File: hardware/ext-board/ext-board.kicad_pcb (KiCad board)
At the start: 2 copper layers, 38.5 x 85 mm, 24 parts, among them J1 GH BM07B link to INT, J2 VCC DATA GND, J3 PTSM 0,5/2-HH-2,5-THR 24 VAC, J4 5V OUT to Pi USB-C, U1 DS2482-100, U2 DS2482-100 (0x19), U3 TMR 12-4811WI

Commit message: Silkscreen: J6 reference below the header, the trunk label beside H1's pin letters
Co-Authored-By: Claude Fable 5.1 <noreply@anthropic.com>
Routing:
- net VCC: track 150.0 -> 177.9 mm, vias 3 -> 1
- net GND: track 167.1 -> 181.6 mm
- net ACR: track 54.0 -> 43.3 mm
- net DATA: track 146.1 -> 138.9 mm
- net GPIO4: track 40.9 -> 46.7 mm
- net SCL: track 74.4 -> 71.6 mm
- net SDA: track 75.1 -> 72.8 mm, vias 2 -> 0
- net H3_DATA: track 15.6 -> 17.5 mm
- net VS: track 72.6 -> 71.2 mm
- net COM: track 48.7 -> 47.7 mm, vias 0 -> 1
- net ACC: vias 1 -> 0
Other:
- board text added: "trunk"
- board text removed: "H1 trunk"

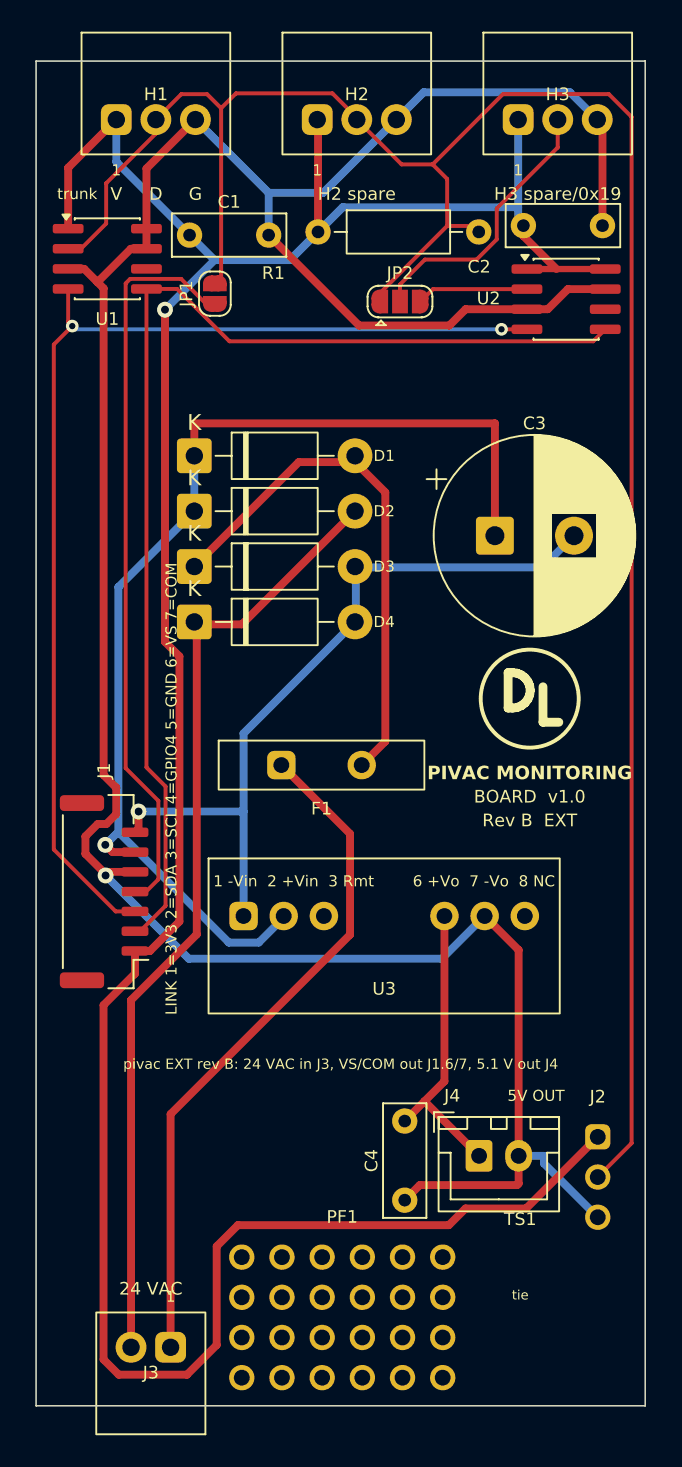
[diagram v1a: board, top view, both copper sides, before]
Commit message: EXT silkscreen: converter pins labelled one by one, R1's reference under R1, link legend beside J1
Co-Authored-By: Claude Fable 5.1 <noreply@anthropic.com>
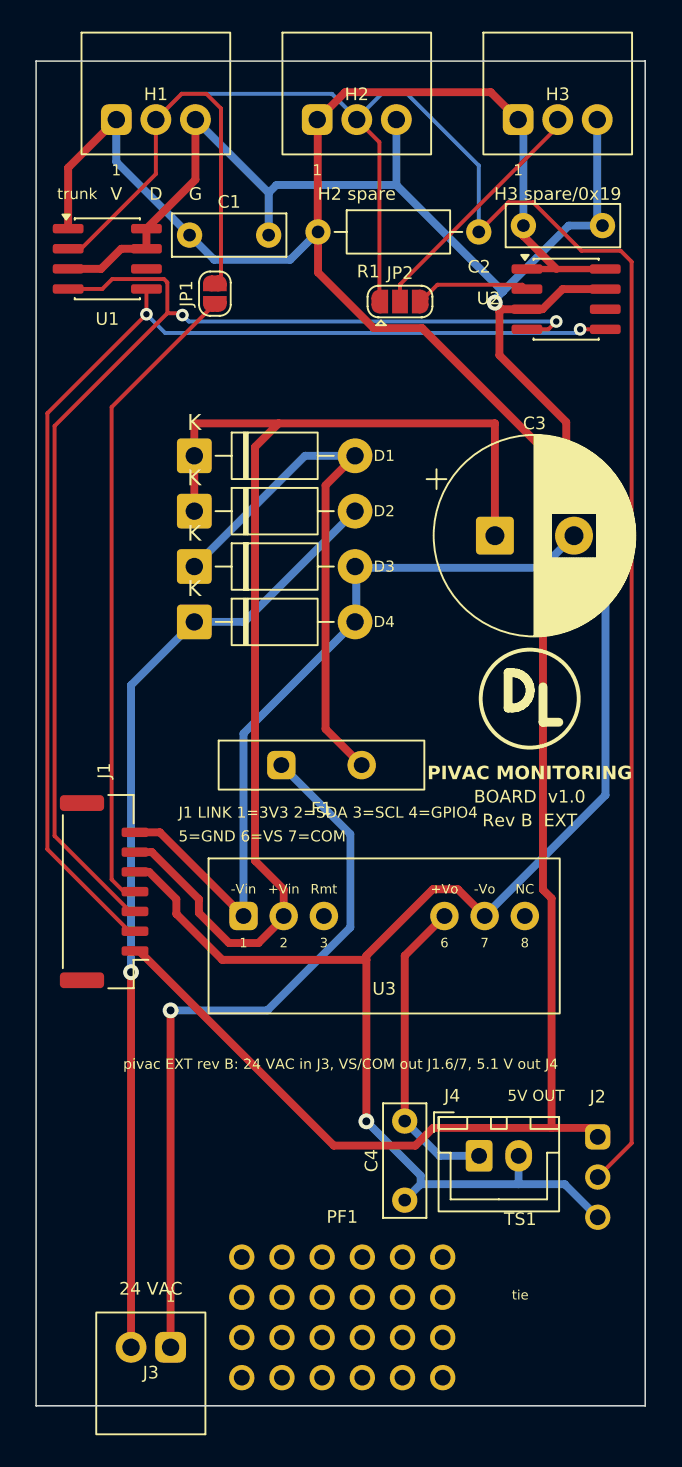
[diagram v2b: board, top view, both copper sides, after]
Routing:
- net VCC: track 177.9 -> 163.1 mm, vias 1 -> 0
- net GND: track 181.6 -> 172.3 mm, vias 1 -> 3
- net SCL: track 71.6 -> 78.5 mm
- net VS: track 71.2 -> 77.2 mm, vias 1 -> 0
- net GPIO4: track 46.7 -> 40.9 mm
- net ACR: track 43.3 -> 46.9 mm, vias 0 -> 1
- net SDA: track 72.8 -> 75.3 mm, vias 0 -> 2
- net H3_DATA: track 17.5 -> 15.6 mm
- net COM: track 47.7 -> 48.7 mm, vias 1 -> 0
- net +5V: track 18.9 -> 19.6 mm
- net ACC: vias 0 -> 1
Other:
- board text added: "5=GND 6=VS 7=COM"
- board text added: "J1 LINK 1=3V3 2=SDA 3=SCL 4=GPIO4"
- board text removed: "LINK 1=3V3 2=SDA 3=SCL 4=GPIO4 5=GND 6=VS 7=COM"

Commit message: EXT silkscreen: R1 and F1 references moved clear, link legend in three lines beside J1
Co-Authored-By: Claude Fable 5.1 <noreply@anthropic.com>
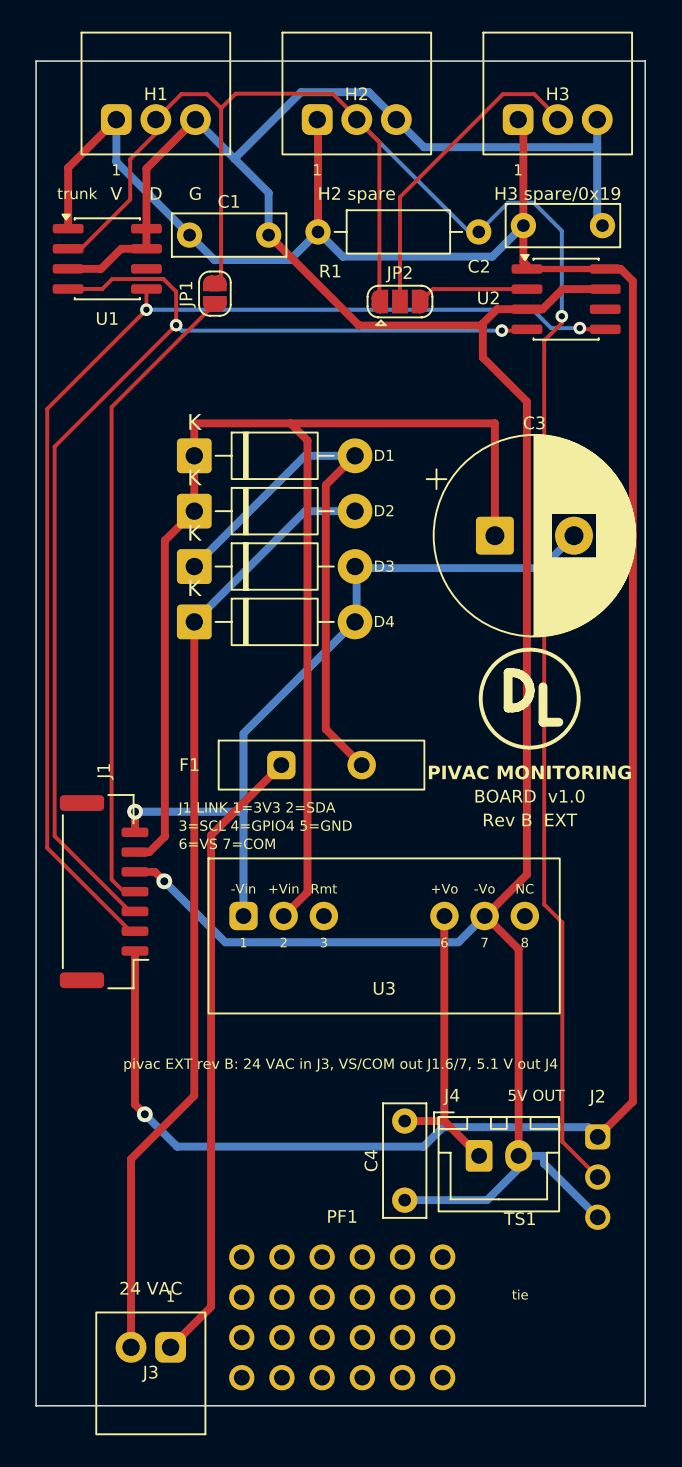
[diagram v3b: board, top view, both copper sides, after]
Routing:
- net DATA: track 138.7 -> 128.2 mm, vias 0 -> 1
- net VS: track 77.2 -> 87.5 mm
- net ACR: track 46.9 -> 39.7 mm, vias 1 -> 0
- net GND: track 172.3 -> 178.1 mm, vias 3 -> 1
- net H3_DATA: track 15.6 -> 20.0 mm
- net SCL: track 78.5 -> 74.4 mm
- net VCC: track 163.1 -> 161.0 mm, vias 0 -> 1
- net +5V: track 19.6 -> 18.6 mm
- net COM: track 48.7 -> 47.8 mm, vias 0 -> 1
- net ACC: vias 1 -> 0
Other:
- board text added: "3=SCL 4=GPIO4 5=GND"
- board text added: "6=VS 7=COM"
- board text added: "J1 LINK 1=3V3 2=SDA"
- board text removed: "5=GND 6=VS 7=COM"
- board text removed: "J1 LINK 1=3V3 2=SDA 3=SCL 4=GPIO4"
